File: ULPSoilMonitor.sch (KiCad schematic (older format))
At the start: 24 parts, among them Q3 BC817, Q4 MMDT3904, SW1 RESET, U1 ESP32-WROOM-32, U2 MCP73123

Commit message: Set charge current to 500mA
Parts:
- JP1, JP2: footprint Jumper:SolderJumper-2_P1.3mm_Open_RoundedPad1.0x1.5mm -> Jumper:SolderJumper-2_P1.3mm_Bridged_RoundedPad1.0x1.5mm; symbol 0-GIE_SMD_Jumpers:SolderJumper_2_Open -> 0-GIE_SMD_Jumpers:SolderJumper_2_Bridged
- gave numbers to parts that had none: 3
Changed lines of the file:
@@
 Set charging current (CP2102N)\nCHREN: 100mA\nCHR0: 500mA (3.9k -> 300mA)\nCHR1: 1.5A (2.37k ->500mA)\n\nOverride pads: \n500mA
 $Comp
-L 0-GIE_SMD_Jumpers:SolderJumper_2_Open JP1
+L 0-GIE_SMD_Jumpers:SolderJumper_2_Bridged JP1
 U 1 1 605B68DB
 P 9200 4600
 F 0 "JP1" V 9154 4668 50  0000 L CNN
 F 1 "Charg_enable" V 9245 4668 50  0001 L CNN
-F 2 "Jumper:SolderJumper-2_P1.3mm_Open_RoundedPad1.0x1.5mm" H 9200 4600 50  0001 C CNN
+F 2 "Jumper:SolderJumper-2_P1.3mm_Bridged_RoundedPad1.0x1.5mm" H 9200 4600 50  0001 C CNN
 F 3 "~" H 9200 4600 50  0001 C CNN
 	1    9200 4600
@@
 $EndComp
 $Comp
-L 0-GIE_SMD_Jumpers:SolderJumper_2_Open JP2
+L 0-GIE_SMD_Jumpers:SolderJumper_2_Bridged JP2
 U 1 1 605B8584
 P 10750 5950
 F 0 "JP2" V 10750 6018 50  0000 L CNN
 F 1 "Charge_500mA" V 10795 6018 50  0001 L CNN
-F 2 "Jumper:SolderJumper-2_P1.3mm_Open_RoundedPad1.0x1.5mm" H 10750 5950 50  0001 C CNN
+F 2 "Jumper:SolderJumper-2_P1.3mm_Bridged_RoundedPad1.0x1.5mm" H 10750 5950 50  0001 C CNN
 F 3 "~" H 10750 5950 50  0001 C CNN
 	1    10750 5950
@@
 	9400 5900 9400 6200
 $Comp
-L 0-GIE_Connector_Debug:USB_C_Receptacle_PowerOnly J?
+L 0-GIE_Connector_Debug:USB_C_Receptacle_PowerOnly J9
 U 1 1 60612B67
 P 8500 1300
-F 0 "J?" H 8607 1817 50  0000 C CNN
+F 0 "J9" H 8607 1817 50  0000 C CNN
 F 1 "USB_C_Receptacle_PowerOnly" H 8607 1726 50  0000 C CNN
 F 2 "0 - GIE Connectors, Terminal Blocks:TYPE-C-31-M-17.kicad_mod" H 8650 1800 50  0001 C CNN
@@
 $EndComp
 $Comp
-L power:GND #PWR?
+L power:GND #PWR0113
 U 1 1 60613D10
 P 8200 2100
-F 0 "#PWR?" H 8200 1850 50  0001 C CNN
+F 0 "#PWR0113" H 8200 1850 50  0001 C CNN
 F 1 "GND" H 8205 1927 50  0000 C CNN
 F 2 "" H 8200 2100 50  0001 C CNN
@@
 $EndComp
 $Comp
-L power:GND #PWR?
+L power:GND #PWR0114
 U 1 1 60614146
 P 8500 2100
-F 0 "#PWR?" H 8500 1850 50  0001 C CNN
+F 0 "#PWR0114" H 8500 1850 50  0001 C CNN
 F 1 "GND" H 8505 1927 50  0000 C CNN
 F 2 "" H 8500 2100 50  0001 C CNN
@@
 $EndComp
 $Comp
-L power:VBUS #PWR?
+L power:VBUS #PWR0115
 U 1 1 6061444E
 P 9100 1150
-F 0 "#PWR?" H 9100 1000 50  0001 C CNN
+F 0 "#PWR0115" H 9100 1000 50  0001 C CNN
 F 1 "VBUS" H 9115 1323 50  0000 C CNN
 F 2 "" H 9100 1150 50  0001 C CNN
@@
 $EndComp
 $Comp
-L Device:R R?
+L Device:R R31
 U 1 1 60614C20
 P 9250 1350
-F 0 "R?" H 9320 1396 50  0000 L CNN
+F 0 "R31" H 9320 1396 50  0000 L CNN
 F 1 "5.1k 10%" H 9320 1305 50  0000 L CNN
 F 2 "Resistor_SMD:R_0805_2012Metric" V 9180 1350 50  0001 C CNN
@@
 $EndComp
 $Comp
-L Device:R R?
+L Device:R R32
 U 1 1 60615957
 P 9250 1450
-F 0 "R?" H 9320 1496 50  0000 L CNN
+F 0 "R32" H 9320 1496 50  0000 L CNN
 F 1 "5.1k 10%" H 9320 1405 50  0000 L CNN
 F 2 "Resistor_SMD:R_0805_2012Metric" V 9180 1450 50  0001 C CNN
@@
 $EndComp
 $Comp
-L power:GND #PWR?
+L power:GND #PWR0116
 U 1 1 60619E98
 P 9450 1500
-F 0 "#PWR?" H 9450 1250 50  0001 C CNN
+F 0 "#PWR0116" H 9450 1250 50  0001 C CNN
 F 1 "GND" H 9455 1327 50  0000 C CNN
 F 2 "" H 9450 1500 50  0001 C CNN

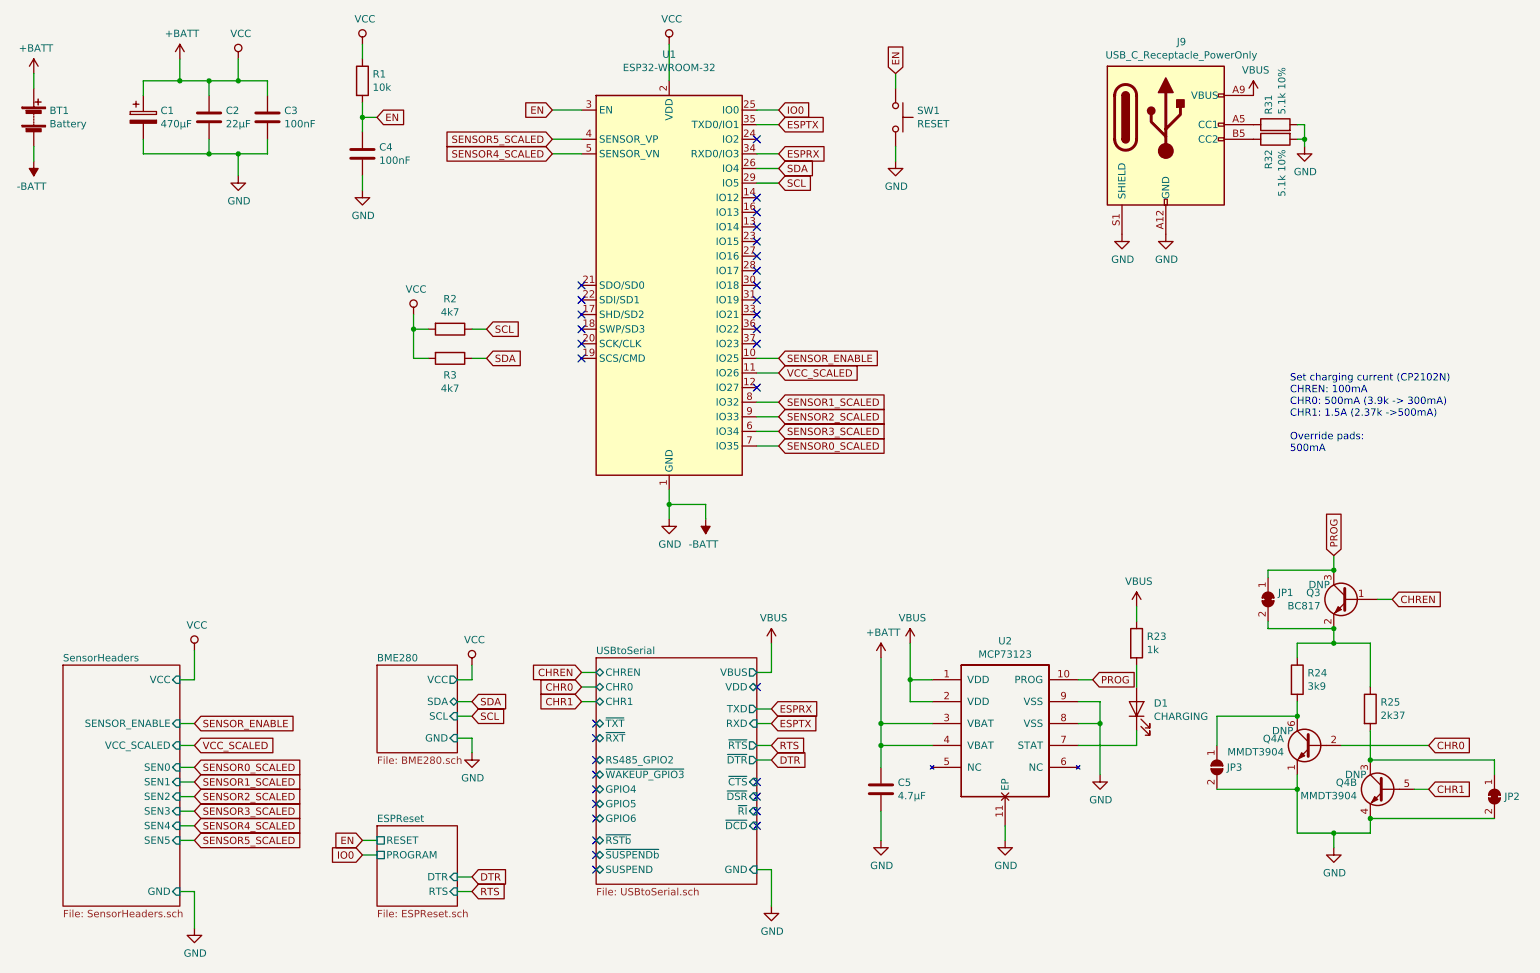
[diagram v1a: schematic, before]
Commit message: Remove USB-serial converter
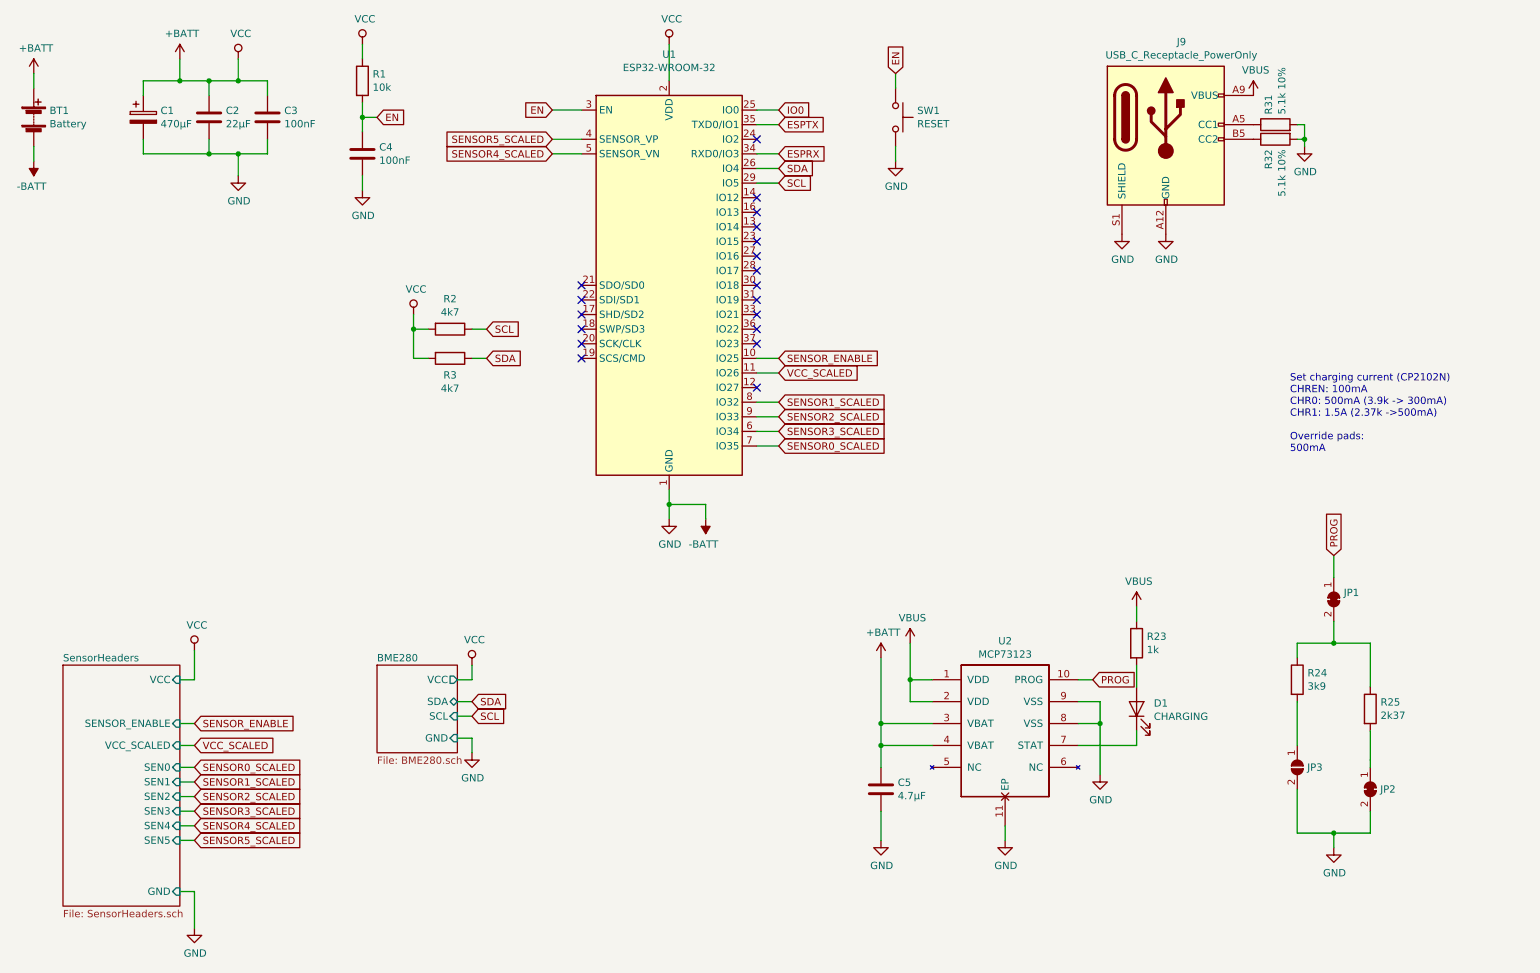
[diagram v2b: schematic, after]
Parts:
- removed Q3: BC817, Package_TO_SOT_SMD:SOT-23, symbol Transistor_BJT:BC817
- removed Q4: MMDT3904, Package_TO_SOT_SMD:SOT-363_SC-70-6, symbol Transistor_BJT:MMDT3904
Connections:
- no-connect marks 34 -> 19
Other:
- moved on the sheet: JP1, JP2, JP3

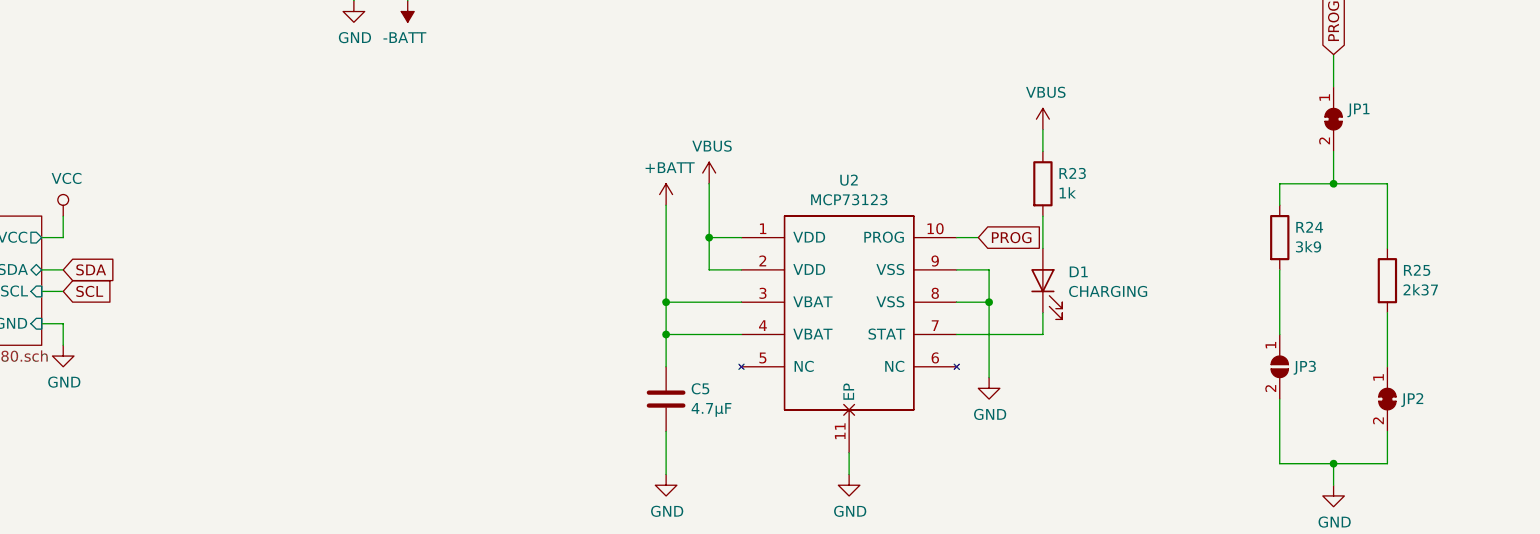
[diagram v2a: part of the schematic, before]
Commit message: Add Tag-Connect for programming
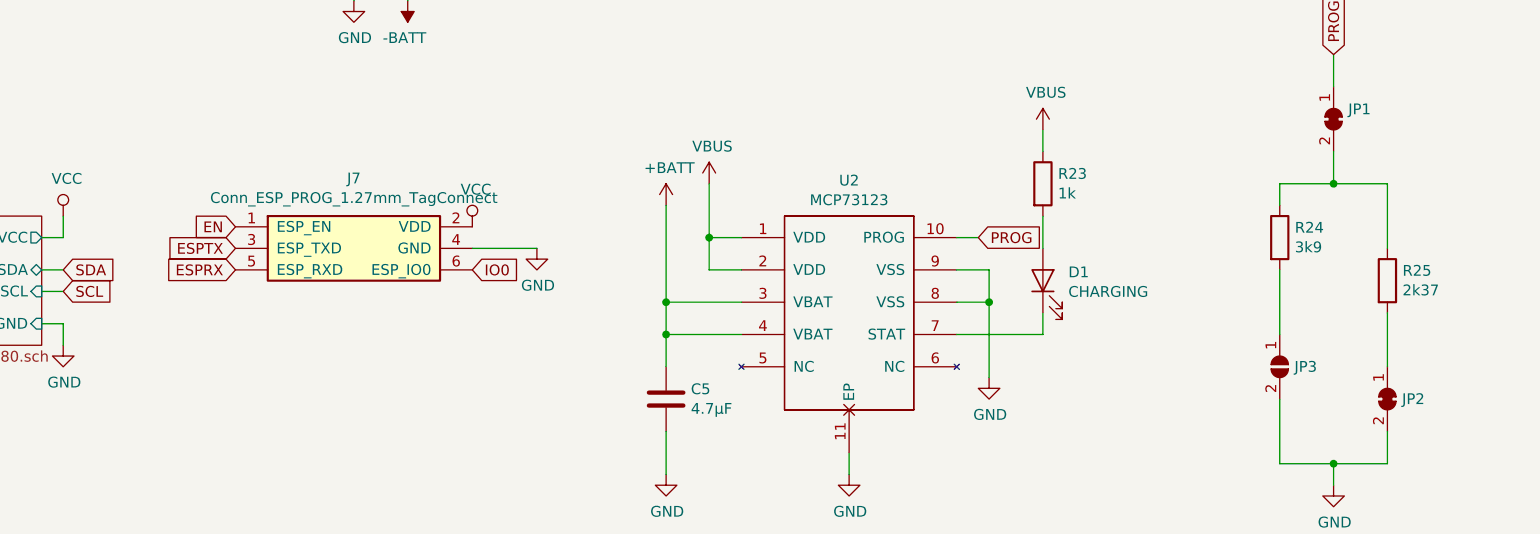
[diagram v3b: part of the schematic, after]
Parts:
- added J7: Conn_ESP_PROG_1.27mm_TagConnect, Connector:Tag-Connect_TC2030-IDC-NL_2x03_P1.27mm_Vertical, symbol 0-GIE_Connector_Debug:Conn_ESP_PROG_1.27mm_TagConnect
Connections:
- net +BATT: now also J7.2 (VDD)
- net -BATT: now also J7.4 (GND)
- net EN: now also J7.1 (ESP_EN)
- net ESPRX: now also J7.5 (ESP_RXD)
- net ESPTX: now also J7.3 (ESP_TXD)
- net IO0: now also J7.6 (ESP_IO0)
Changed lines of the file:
@@
 Text GLabel 9650 4300 1    50   Input ~ 0
 PROG
-Wire Wire Line
-	9900 5700 9900 5500
 $Comp
 L power:+BATT #PWR0112
@@
 	0    1    1    0
 $EndComp
-Wire Wire Line
-	9900 5750 9900 5700
 $Comp
 L Device:R R24
@@
 Wire Wire Line
 	9400 5300 9400 5600
+$Comp
+L 0-GIE_Connector_Debug:Conn_ESP_PROG_1.27mm_TagConnect J7
+U 1 1 6067D97D
+P 5100 5200
+F 0 "J7" H 5100 5525 50  0000 C CNN
+F 1 "Conn_ESP_PROG_1.27mm_TagConnect" H 5100 5434 50  0000 C CNN
+F 2 "Connector:Tag-Connect_TC2030-IDC-NL_2x03_P1.27mm_Vertical" H 5150 4900 50  0001 C CNN
+F 3 "~" H 5100 5200 50  0001 C CNN
+	1    5100 5200
+	1    0    0    -1
+$EndComp
+$Comp
+L power:GND #PWR0108
+U 1 1 6067ECC5
+P 5950 5200
+F 0 "#PWR0108" H 5950 4950 50  0001 C CNN
+F 1 "GND" H 5955 5027 50  0000 C CNN
+F 2 "" H 5950 5200 50  0001 C CNN
+F 3 "" H 5950 5200 50  0001 C CNN
+	1    5950 5200
+	1    0    0    -1
+$EndComp
+Wire Wire Line
+	5650 5200 5950 5200
+Wire Wire Line
+	9900 5500 9900 5750
+Text GLabel 5650 5300 2    50   Input ~ 0
+IO0
+$Comp
+L power:VCC #PWR0109
+U 1 1 6068214D
+P 5650 5100
+F 0 "#PWR0109" H 5650 4950 50  0001 C CNN
+F 1 "VCC" H 5667 5273 50  0000 C CNN
+F 2 "" H 5650 5100 50  0001 C CNN
+F 3 "" H 5650 5100 50  0001 C CNN
+	1    5650 5100
+	1    0    0    -1
+$EndComp
+Text GLabel 4550 5200 0    50   Input ~ 0
+ESPTX
+Text GLabel 4550 5300 0    50   Input ~ 0
+ESPRX
+Text GLabel 4550 5100 0    50   Input ~ 0
+EN
 $EndSCHEMATC
